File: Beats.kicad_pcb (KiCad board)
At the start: 2 copper layers, 60 x 106.5 mm, 117 parts, among them J1 AudioJack2_SwitchT, J10 AudioJack2_SwitchT, J11 AudioJack2_SwitchT, J12 AudioJack2_SwitchT, J13 AudioJack2_SwitchT, J14 AudioJack2_SwitchT, J15 AudioJack2_SwitchT, J16 AudioJack2_SwitchT, J17 Conn_02x05_Odd_Even, J18 UART, J2 AudioJack2_SwitchT, J3 AudioJack2_SwitchT, J4 AudioJack2_SwitchT, J5 AudioJack2_SwitchT, J6 AudioJack2_SwitchT, J7 SWD, J8 Conn_01x03_Male, J9 AudioJack2_SwitchT, Q1 BC847, Q10 BC847, Q11 BC847, Q12 BC847, Q13 BC847, Q2 BC847, Q3 BC847, Q4 BC847, Q5 BC847, Q6 BC847, Q7 BC847, Q8 BC847, Q9 BC847, SW1 Rotary_Encoder_Switch, SW10 SW_Push_LED, SW11 SW_Push_LED, SW12 SW_Push_LED, SW13 SW_Push_LED, SW2 SW_Push, SW3 SW_Push_LED, SW4 SW_Push_LED, SW5 SW_Push_LED, SW6 SW_Push_LED, SW7 SW_Push_LED, SW8 SW_Push_LED, SW9 SW_Push_LED, U1 MCP6004, U2 IPS240x240, U3 STM32F051R8Tx, U4 AT25xxx, U5 74AHCT244, U6 L7805, U7 LM1117-3.3, Y1 8MHz

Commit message: All pins assigned and connected.
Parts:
- added D5: LED, LED_SMD:LED_0603_1608Metric_Castellated, F.Cu at (125.2, 51.0)
- added D6: LED, LED_SMD:LED_0603_1608Metric_Castellated, F.Cu at (127.8, 51.0)
- added Q14: BC847, Package_TO_SOT_SMD:SOT-23, F.Cu at (131.6, 55.5)
- added Q15: BC847, Package_TO_SOT_SMD:SOT-23, F.Cu at (135.8, 55.5)
- added R41: 47, Resistor_SMD:R_0603_1608Metric, F.Cu at (125.2, 54.7)
- added R42: 47, Resistor_SMD:R_0603_1608Metric, F.Cu at (127.8, 54.7)
- D4: footprint LED_SMD:LED_1206_3216Metric_Castellated -> LED_SMD:LED_0603_1608Metric_Castellated
- moved R25 3.74 mm to (122.7, 54.7)
- moved J8 2.81 mm to (129.9, 59.4)
- moved D4 2.67 mm to (122.7, 51.0)
- moved Q4 0.13 mm to (162.4, 68.4)
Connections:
- R2 pad 2: GND -> Net-(J1-PadT)
- R4 pad 2: GND -> Net-(J2-PadT)
- R6 pad 2: GND -> Net-(J3-PadT)
- R8 pad 2: GND -> Net-(J4-PadT)
- SW1 pad S1: Net-(SW1-PadS1) -> PB6
- U4 pad 7: +3.3VA -> PB7

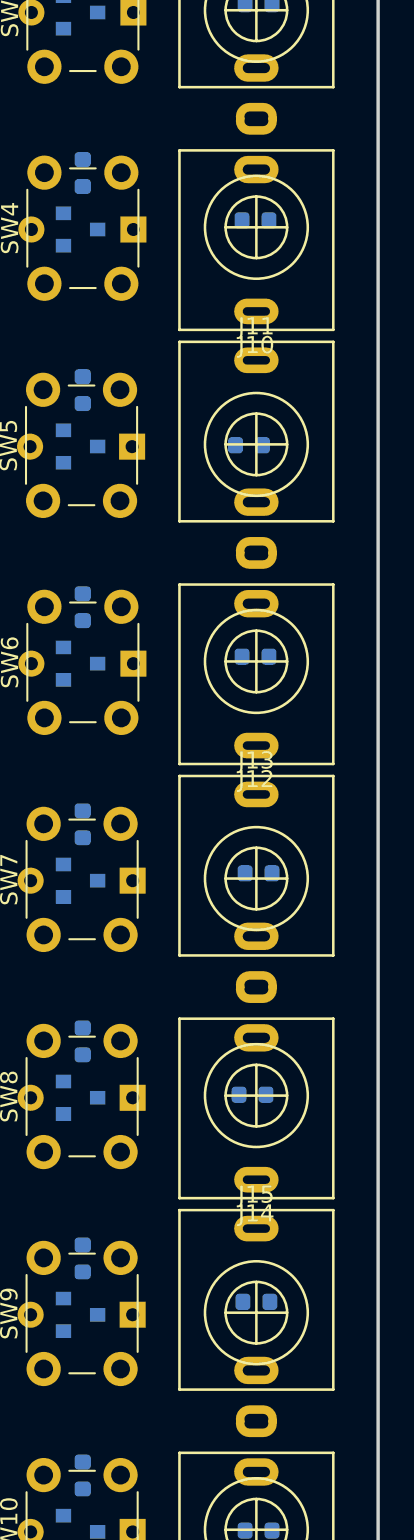
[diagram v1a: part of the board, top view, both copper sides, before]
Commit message: Shared pads adjusment, four-layers and ground-plane fill.
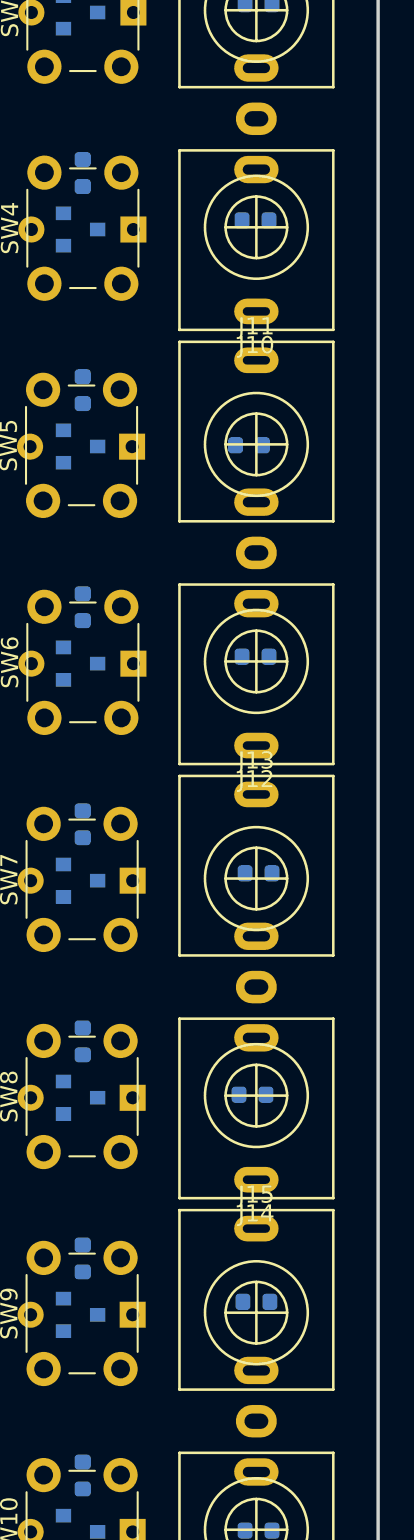
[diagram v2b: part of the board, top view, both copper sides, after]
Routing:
- added copper zone on In2.Cu, net GND
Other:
- copper layers 2 -> 4

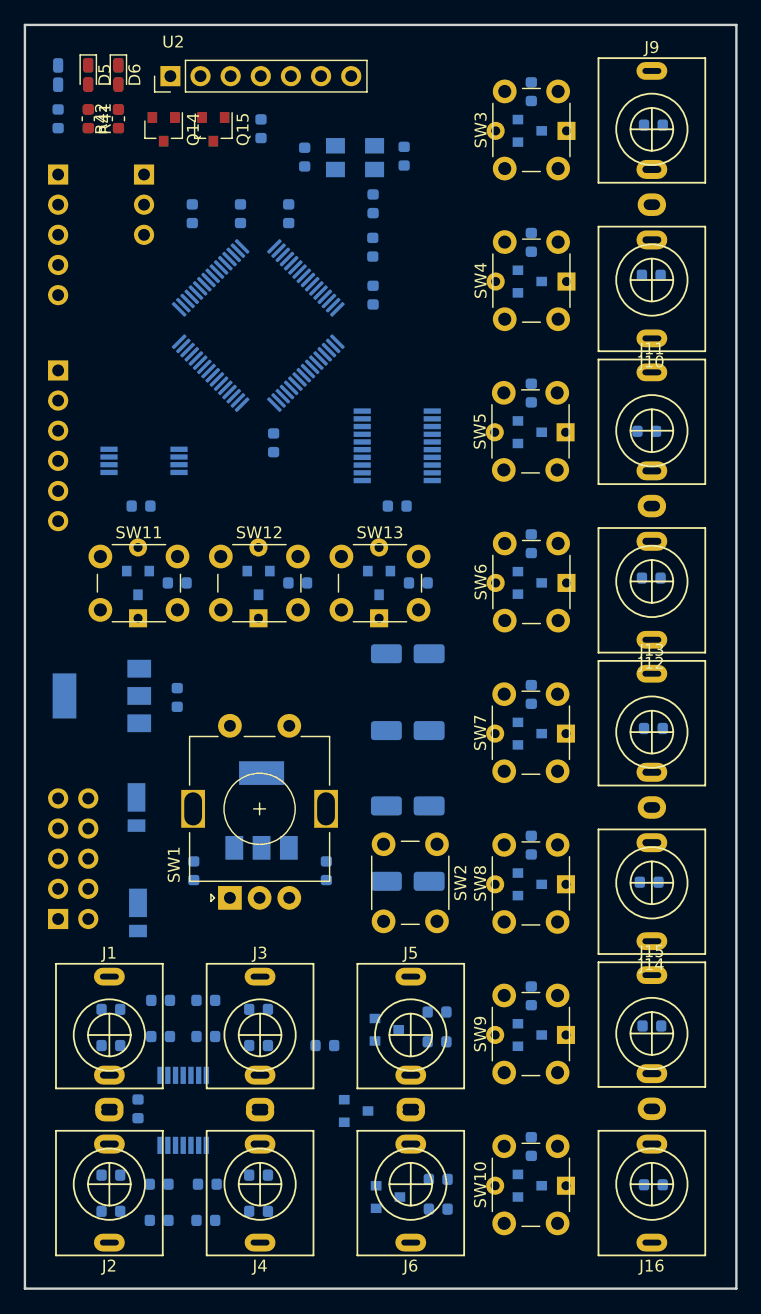
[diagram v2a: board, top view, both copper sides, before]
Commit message: Improved component placement.
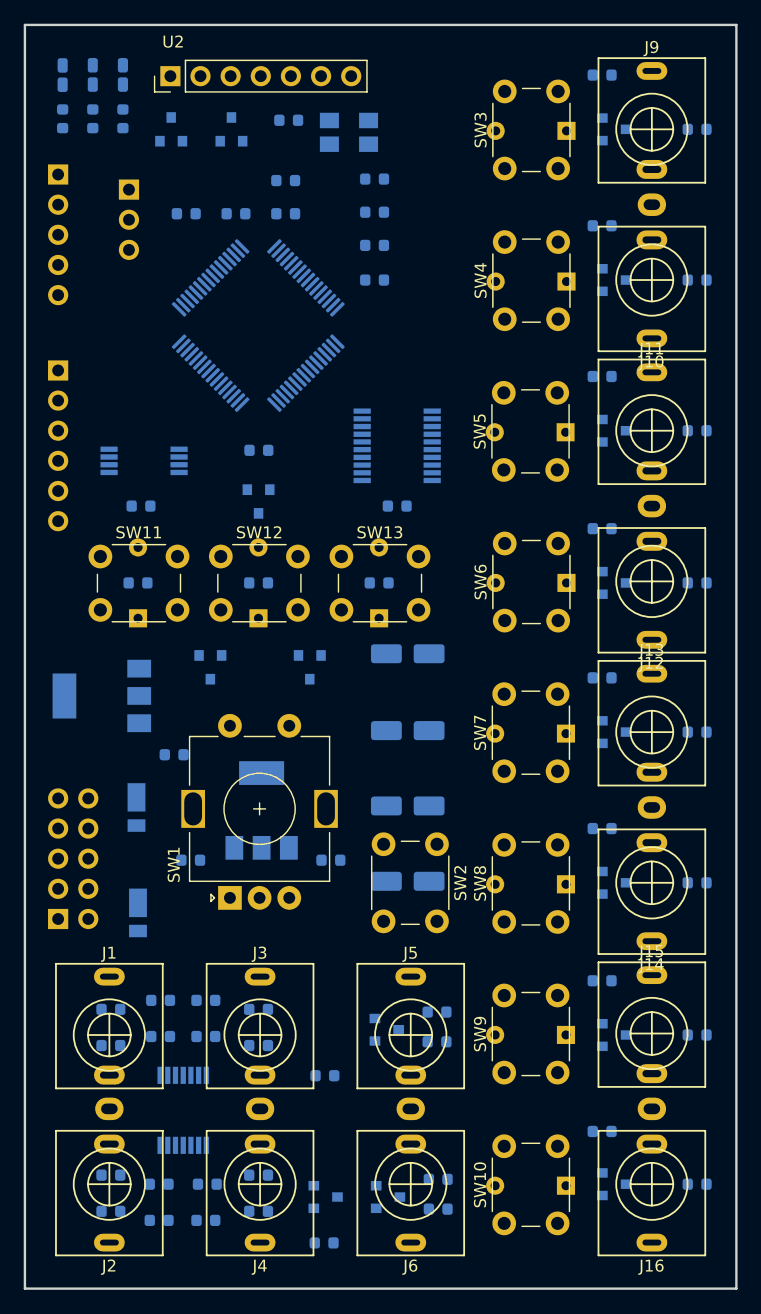
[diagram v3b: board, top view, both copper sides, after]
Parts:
- D5, D6, Q14, Q15, R41, R42: moved to B.Cu
- moved R24 16.6 mm to (145.1, 149.4)
- moved C14 16.0 mm to (145.2, 135.3), turned to 0 degrees
- moved Q11 9.37 mm to (135.5, 100.9)
- moved Q13 9.20 mm to (143.9, 100.9)
- moved D1 7.69 mm to (145.2, 145.5)
- moved Q10 7.11 mm to (169.6, 144.4)
- moved Q7 7.11 mm to (169.6, 106.3)
- moved Q8 7.11 mm to (169.6, 119.0)
- moved Q3 7.11 mm to (169.6, 55.5)
- moved Q4 7.11 mm to (169.6, 68.2)
- moved Q5 7.11 mm to (169.6, 81.0)
- moved Q6 7.11 mm to (169.6, 93.8)
- moved Q9 7.11 mm to (169.6, 131.9)
- moved Q12 6.86 mm to (139.6, 86.9)
- moved R31 6.13 mm to (168.5, 63.7), turned to 0 degrees
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
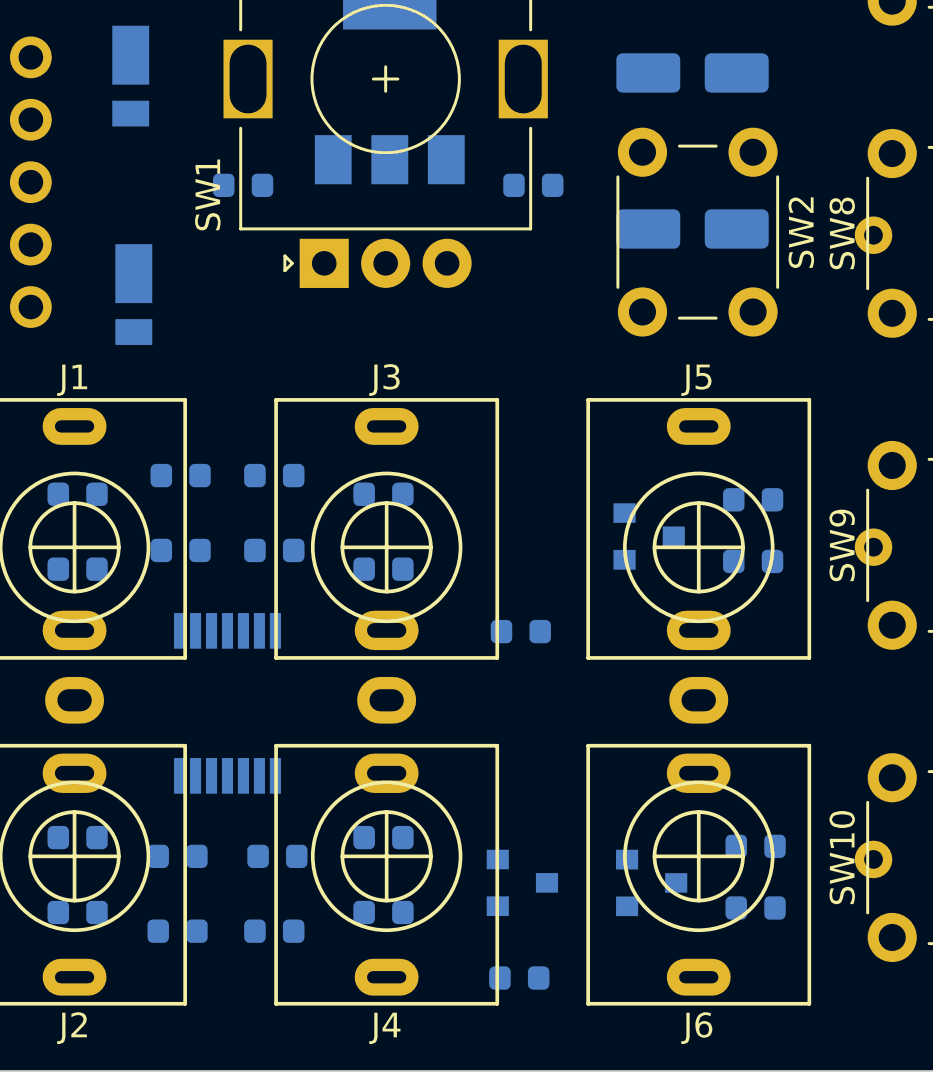
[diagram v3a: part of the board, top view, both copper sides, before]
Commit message: Fixed wrong voltage on clock / reset inputs and better wiring.
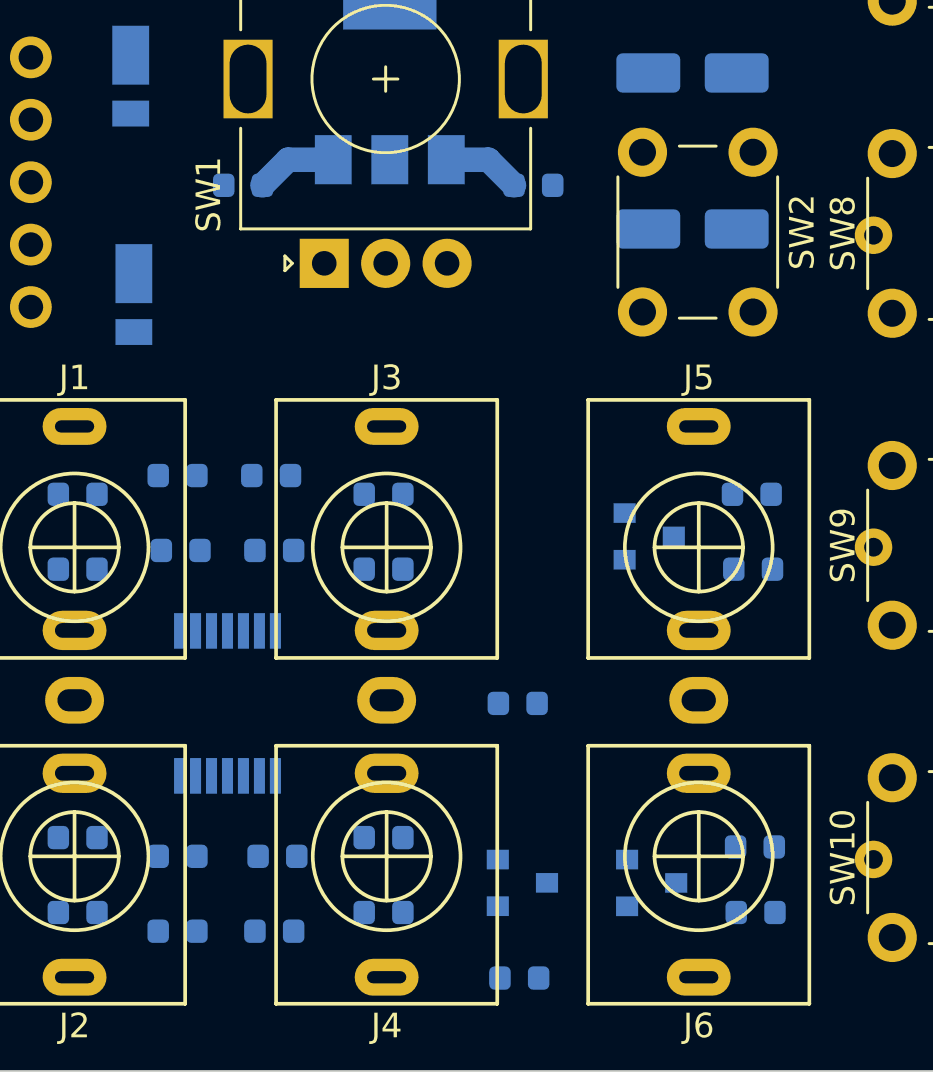
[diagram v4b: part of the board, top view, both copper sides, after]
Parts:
- moved R1 12.4 mm to (127.1, 132.8)
- moved R2 12.4 mm to (127.1, 129.7)
- moved R3 12.4 mm to (139.6, 132.8)
- moved R4 12.4 mm to (139.6, 129.7)
- moved C1 3.94 mm to (131.2, 129.0)
- moved C2 3.68 mm to (135.0, 129.0)
- moved C14 2.92 mm to (145.0, 138.2)
- moved R26 2.82 mm to (154.6, 132.8), turned to 180 degrees
- moved R27 2.73 mm to (154.6, 129.7), turned to 180 degrees
- moved R28 2.69 mm to (154.7, 146.7), turned to 180 degrees
- moved R29 2.48 mm to (154.7, 144.1), turned to 180 degrees
- turned C19 to 180 degrees
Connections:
- R27 pad 1: +5V -> +3.3VA
- R29 pad 1: +5V -> +3.3VA
- R4 pad 2: Net-(J2-PadT) -> Net-(J3-PadT)
- R6 pad 2: Net-(J3-PadT) -> Net-(J4-PadT)
- R8 pad 2: Net-(J4-PadT) -> Net-(J2-PadT)
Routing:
- net +5V: track 0.00 -> 3.31 mm
- net +12V: track 0.00 -> 3.19 mm

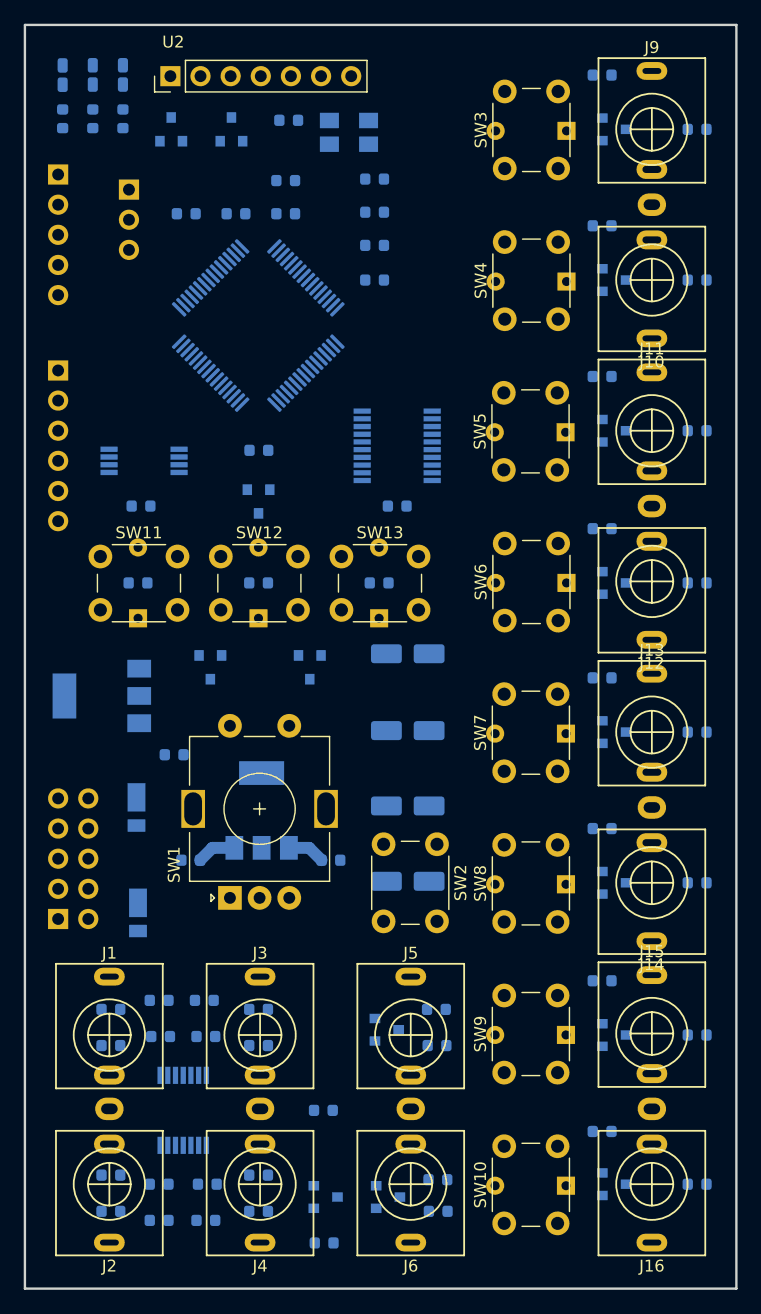
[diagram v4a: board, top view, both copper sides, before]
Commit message: Power and ground planes routed and poured.
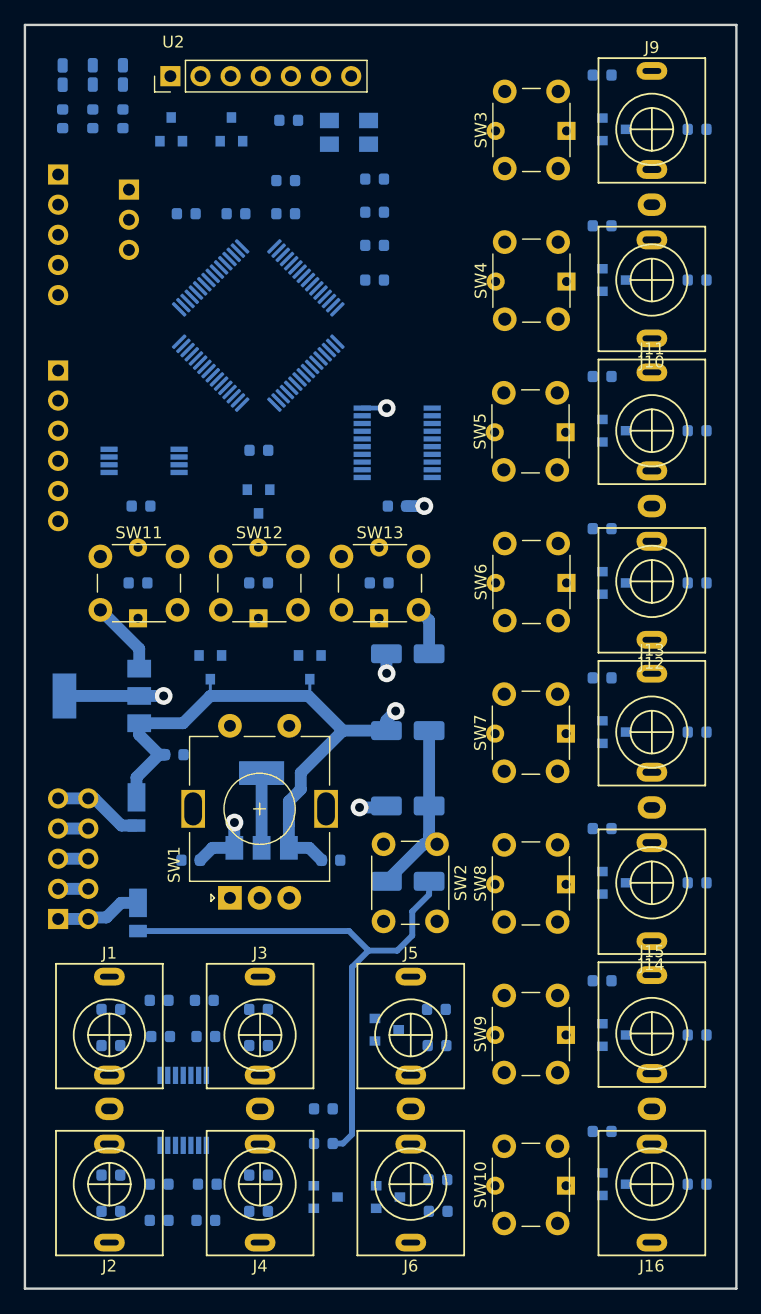
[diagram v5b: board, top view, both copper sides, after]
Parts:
- moved R24 8.38 mm to (145.0, 141.0), turned to 180 degrees
- moved U5 0.25 mm to (151.3, 82.0)
- moved C14 0.13 mm to (145.0, 138.1)
- turned C9 to 180 degrees
- turned R1 to 0 degrees
- turned R3 to 0 degrees
- turned R5 to 0 degrees
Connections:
- C15 pad 1: +12V -> +5V
- C16 pad 1: GND -> +12V
- C16 pad 2: -12V -> GND
- C20 pad 1: +3.3VA -> GND
- C20 pad 2: GND -> -12V
- C21 pad 1: +5V -> +3.3VA
- J5 pad TN: +5V -> +3.3VA
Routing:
- net +12V: track 3.19 -> 207.1 mm, vias 0 -> 1
- net +5V: track 3.31 -> 68.0 mm, vias 0 -> 4
- net -12V: track 0.00 -> 47.5 mm
- net GND: track 0.00 -> 39.7 mm
- net +3.3VA: track 0.00 -> 10.0 mm, vias 0 -> 2
- net Net-(D2-Pad2): track 0.00 -> 7.55 mm
- net Net-(D3-Pad1): track 0.00 -> 7.29 mm
- added copper zone on In1.Cu, net +3.3VA
- added copper zone on In1.Cu, net GND
